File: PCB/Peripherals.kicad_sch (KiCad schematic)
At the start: 0 parts

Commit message: ADD: Ethernet
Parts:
- added J3: USB4216-03-A, USB421603A, symbol SamacSys_Parts:USB4216-03-A
- added J6: SS-90000-009, SS90000009, symbol SamacSys_Parts:SS-90000-009
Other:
- note added: "Ethernet"
- note added: "USB C"

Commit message: Add: Ethernet
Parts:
- added C14, C15, C16, C17, C18, C20: 100nF, CAPC1608X90N, symbol SamacSys_Parts:CC0603KRX7R7BB104
- added C19: 10uF, CAPPM3216X180N, symbol SamacSys_Parts:TAJA106K016R
- added C21: 1uF, CAPC1608X90N, symbol SamacSys_Parts:CC0603KRX5R7BB105
- added C22: 470pF, CAPC1608X90N, symbol SamacSys_Parts:CC0603JRNPO9BN471
- added C23: 1nF, CAPC3216X145N, symbol SamacSys_Parts:CC1206KKX7RDBB102
- added FB1: BEAD, BEADC1608X95N, symbol SamacSys_Parts:FCM1608KF-601T05
- added IC3: LAN8742A-CZ-TR, QFN50P400X400X100-25N-D, symbol SamacSys_Parts:LAN8742A-CZ-TR
- added IC4: USBLC6-4SC6, SOT95P280X145-6N, symbol SamacSys_Parts:USBLC6-4SC6
- added JP4, JP5: Jumper_2_Open, symbol Jumper:Jumper_2_Open
- added R11, R13, R14, R15, R16, R32: 10K, RESC1608X50N, symbol SamacSys_Parts:CRCW060310K0FKEI
- added R17, R18, R19, R20: 33, RESC1608X55N, symbol SamacSys_Parts:CRG0603F33R
- added R21: 1K5, RESC1608X50N, symbol SamacSys_Parts:CRCW06031K50FKED
- added R22: 0, RESC1608X50N, symbol SamacSys_Parts:CRCW06030000Z0EI
- added R23: 12K1, RESC1609X55N, symbol SamacSys_Parts:ERJ-P03F1212V
- added R24, R25, R26, R27: 50, RESC1608X55N, symbol SamacSys_Parts:TNPW060350R0DEEA
- added R28, R29, R30, R31: 75, RESC1608X55N, symbol SamacSys_Parts:RC0603FR-0775RL
- added R33, R34: 270, RESC1608X55N, symbol SamacSys_Parts:RC0603FR-07270RL
- added T1: H1102NL, SOIC127P940X597-16N, symbol SamacSys_Parts:H1102NL
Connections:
- net at J6.1: now also T1.16 (TX+)
- net at J6.10 (A_GREEN): now also IC3.2 (LED2/NINT/NPME/NINTSEL), R32.2
- net at J6.11 (K_YELLOW): now also R34.2
- net at J6.12 (A_YELLOW): now also C14.1, C15.1, C16.2, C17.2, C18.2, C19.1 (+), FB1.2, IC3.19 (VDD1A), IC3.3 (LED1/NINT/NPME/REGOFF), IC4.5 (VBUS), R24.2, R25.2, R26.2, R27.2, T1.2 (CT_1), T1.7 (CT_2)
- net at J6.2: now also T1.14 (TX-)
- net at J6.3: now also T1.11 (RX+)
- net at J6.4: now also J6.5, R29.2, R30.2, T1.15 (NC_6)
- net at J6.6: now also T1.9 (RX-)
- net at J6.7: now also J6.8, R31.2
- net at J6.9 (K_GREEN): now also R33.2
- net GNDPWR: now reaches J6.MH3
- net GNDPWR: now also J6.MH4, C23.1, JP4.1 (A), JP5.1 (A)
- net GNDREF: now reaches J3.A1 (GND_1)
- net GNDREF: now also J3.B1 (GND_2), J3.G1 (GND_3), J3.G2 (GND_4), J3.G3 (GND_5), J3.G4 (GND_6), C14.2, C15.2, C16.1, C17.1, C18.1, C19.2 (-), C20.1, C21.2, C22.2, IC3.25 (EP), IC4.2 (GND), JP4.2 (B), JP5.2 (B), R11.1, R23.2, R32.1, R33.1, R34.1
- net 5V: now reaches J3.A4 (VBUS_1)
- net 5V: now also J3.B4 (VBUS_2)
- new net: IC3.8 (RXD0/MODE0), R14.2, R17.2
- new net: IC3.22 (RXN), IC4.6 (I/O4), R24.1, T1.8 (RD-)
- new net: IC3.11 (CRS_DV/MODE2), R15.2, R19.1
- new net: C23.2, R28.1, R29.1, R30.1, R31.1
- new net: IC3.21 (TXP), IC4.3 (I/O2), R25.1, T1.1 (TD+)
- new net: R28.2, T1.10 (NC_3)
- new net: IC3.20 (TXN), IC4.4 (I/O3), R26.1, T1.3 (TD-)
- new net: IC3.23 (RXP), IC4.1 (I/O1), R27.1, T1.6 (RD+)
- new net: IC3.7 (RXD1/MODE1), R13.2, R18.2
- new net: IC3.10 (RXER/PHYAD0), R11.2
- new net: IC3.14 (NINT/REFCLKO), R16.2, R20.1
- new net: IC3.15 (NRST), R22.1
- new net: IC3.24 (RBIAS), R23.1
- new net: C21.1, C22.1, IC3.6 (VDDCR)
- new net +3V3_PER: C20.2, FB1.1, IC3.9 (VDDIO), R13.1, R14.1, R15.1, R16.1, R21.1
- new net NRST: R22.2
- new net PHY_CLK_25MHZ: IC3.5 (XTAL1/CLKIN)
- new net RMII_CRX_DV: R19.2
- new net RMII_MDC: IC3.13 (MDC)
- new net RMII_MDIO: IC3.12 (MDIO), R21.2
- new net RMII_REF_CLK: R20.2
- new net RMII_RXD0: R17.1
- new net RMII_RXD1: R18.1
- new net RMII_TXD0: IC3.17 (TXD0)
- new net RMII_TXD1: IC3.18 (TXD1)
- new net RMII_TX_EN: IC3.16 (TXEN)
- no-connect marks 0 -> 9
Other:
- note added: "CC1 fait parti de la norme ??"
- note added: "Ne pas oublier pair différentiel !?"
- moved on the sheet: J3, J6

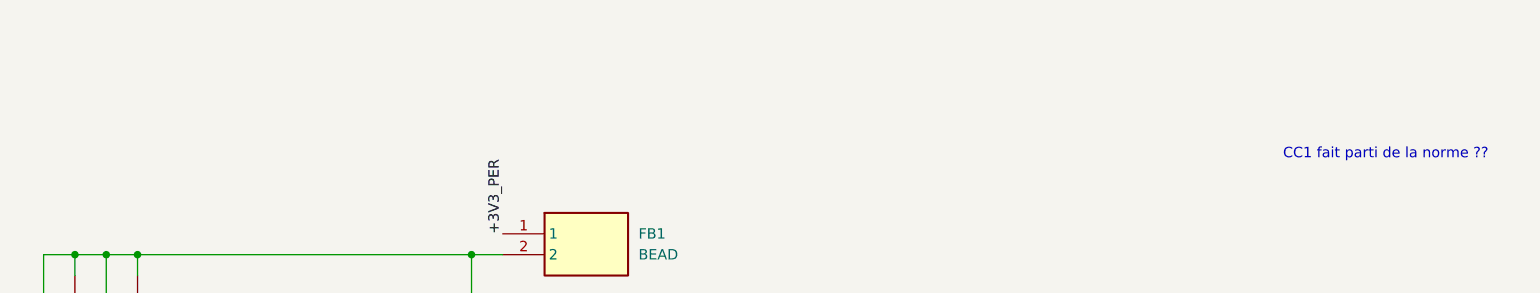
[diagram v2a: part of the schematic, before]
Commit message: List of Modifs:
Corrected power supply sheet
Updated motor driver sheet
Added a project name to a lot of sheets (don't know why...)
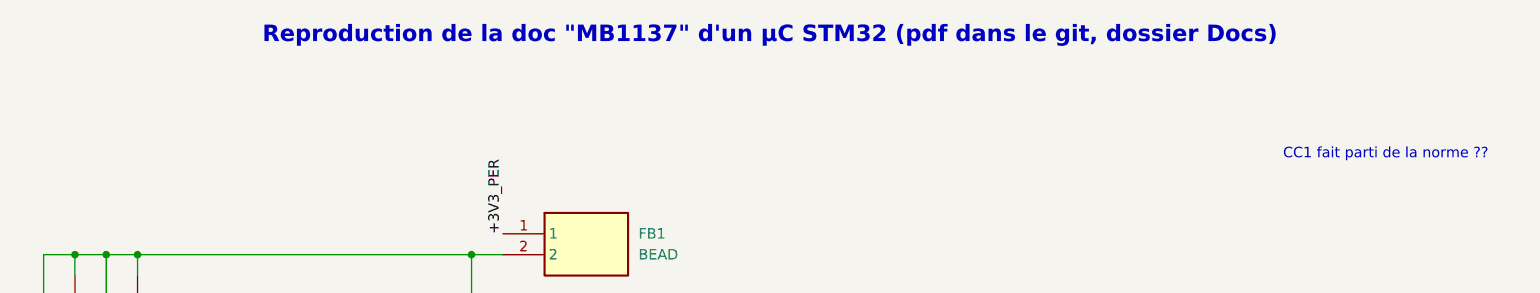
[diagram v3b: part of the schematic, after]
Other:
- note added: "Reproduction de la doc "MB1137" d'un µC STM32 (pdf dans le git, dossier Docs)"
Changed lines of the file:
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@@
 		)
 	)
+	(text "Reproduction de la doc \"MB1137\" d'un µC STM32 (pdf dans le git, dossier Docs)"
+		(exclude_from_sim no)
+		(at 144.272 16.51 0)
+		(effects
+			(font
+				(size 2 2)
+				(thickness 0.6)
+				(bold yes)
+			)
+		)
+	)
 	(text "CC1 fait parti de la norme ??"
 		(exclude_from_sim no)
@@
 		)
 		(instances
-			(project ""
+			(project "PCB"
 				(path "/117fd49e-499d-4b54-b58c-f6b538ecca4a/b9176f6a-4299-4bca-a59b-5ff3df09c616/6ae8cb66-0d01-49c6-940e-175426e825e5"
 					(reference "#PWR037")
@@
 		)
 		(instances
-			(project ""
+			(project "PCB"
 				(path "/117fd49e-499d-4b54-b58c-f6b538ecca4a/b9176f6a-4299-4bca-a59b-5ff3df09c616/6ae8cb66-0d01-49c6-940e-175426e825e5"
 					(reference "R24")
@@
 		)
 		(instances
-			(project ""
+			(project "PCB"
 				(path "/117fd49e-499d-4b54-b58c-f6b538ecca4a/b9176f6a-4299-4bca-a59b-5ff3df09c616/6ae8cb66-0d01-49c6-940e-175426e825e5"
 					(reference "C23")
@@
 		)
 		(instances
-			(project ""
+			(project "PCB"
 				(path "/117fd49e-499d-4b54-b58c-f6b538ecca4a/b9176f6a-4299-4bca-a59b-5ff3df09c616/6ae8cb66-0d01-49c6-940e-175426e825e5"
 					(reference "T1")
@@
 		)
 		(instances
-			(project ""
+			(project "PCB"
 				(path "/117fd49e-499d-4b54-b58c-f6b538ecca4a/b9176f6a-4299-4bca-a59b-5ff3df09c616/6ae8cb66-0d01-49c6-940e-175426e825e5"
 					(reference "IC3")
@@
 		)
 		(instances
-			(project ""
+			(project "PCB"
 				(path "/117fd49e-499d-4b54-b58c-f6b538ecca4a/b9176f6a-4299-4bca-a59b-5ff3df09c616/6ae8cb66-0d01-49c6-940e-175426e825e5"
 					(reference "R21")
@@
 		)
 		(instances
-			(project ""
+			(project "PCB"
 				(path "/117fd49e-499d-4b54-b58c-f6b538ecca4a/b9176f6a-4299-4bca-a59b-5ff3df09c616/6ae8cb66-0d01-49c6-940e-175426e825e5"
 					(reference "#PWR044")
@@
 		)
 		(instances
-			(project ""
+			(project "PCB"
 				(path "/117fd49e-499d-4b54-b58c-f6b538ecca4a/b9176f6a-4299-4bca-a59b-5ff3df09c616/6ae8cb66-0d01-49c6-940e-175426e825e5"
 					(reference "C21")
@@
 		)
 		(instances
-			(project ""
+			(project "PCB"
 				(path "/117fd49e-499d-4b54-b58c-f6b538ecca4a/b9176f6a-4299-4bca-a59b-5ff3df09c616/6ae8cb66-0d01-49c6-940e-175426e825e5"
 					(reference "J6")
@@
 		)
 		(instances
-			(project ""
+			(project "PCB"
 				(path "/117fd49e-499d-4b54-b58c-f6b538ecca4a/b9176f6a-4299-4bca-a59b-5ff3df09c616/6ae8cb66-0d01-49c6-940e-175426e825e5"
 					(reference "R17")
@@
 		)
 		(instances
-			(project ""
+			(project "PCB"
 				(path "/117fd49e-499d-4b54-b58c-f6b538ecca4a/b9176f6a-4299-4bca-a59b-5ff3df09c616/6ae8cb66-0d01-49c6-940e-175426e825e5"
 					(reference "FB1")
@@
 		)
 		(instances
-			(project ""
+			(project "PCB"
 				(path "/117fd49e-499d-4b54-b58c-f6b538ecca4a/b9176f6a-4299-4bca-a59b-5ff3df09c616/6ae8cb66-0d01-49c6-940e-175426e825e5"
 					(reference "IC4")
@@
 		)
 		(instances
-			(project ""
+			(project "PCB"
 				(path "/117fd49e-499d-4b54-b58c-f6b538ecca4a/b9176f6a-4299-4bca-a59b-5ff3df09c616/6ae8cb66-0d01-49c6-940e-175426e825e5"
 					(reference "R22")
@@
 		)
 		(instances
-			(project ""
+			(project "PCB"
 				(path "/117fd49e-499d-4b54-b58c-f6b538ecca4a/b9176f6a-4299-4bca-a59b-5ff3df09c616/6ae8cb66-0d01-49c6-940e-175426e825e5"
 					(reference "JP4")
@@
 		)
 		(instances
-			(project ""
+			(project "PCB"
 				(path "/117fd49e-499d-4b54-b58c-f6b538ecca4a/b9176f6a-4299-4bca-a59b-5ff3df09c616/6ae8cb66-0d01-49c6-940e-175426e825e5"
 					(reference "C22")
@@
 		)
 		(instances
-			(project ""
+			(project "PCB"
 				(path "/117fd49e-499d-4b54-b58c-f6b538ecca4a/b9176f6a-4299-4bca-a59b-5ff3df09c616/6ae8cb66-0d01-49c6-940e-175426e825e5"
 					(reference "J3")
@@
 		)
 		(instances
-			(project ""
+			(project "PCB"
 				(path "/117fd49e-499d-4b54-b58c-f6b538ecca4a/b9176f6a-4299-4bca-a59b-5ff3df09c616/6ae8cb66-0d01-49c6-940e-175426e825e5"
 					(reference "R23")
@@
 		)
 		(instances
-			(project ""
+			(project "PCB"
 				(path "/117fd49e-499d-4b54-b58c-f6b538ecca4a/b9176f6a-4299-4bca-a59b-5ff3df09c616/6ae8cb66-0d01-49c6-940e-175426e825e5"
 					(reference "R33")
@@
 		)
 		(instances
-			(project ""
+			(project "PCB"
 				(path "/117fd49e-499d-4b54-b58c-f6b538ecca4a/b9176f6a-4299-4bca-a59b-5ff3df09c616/6ae8cb66-0d01-49c6-940e-175426e825e5"
 					(reference "C19")
@@
 		)
 		(instances
-			(project ""
+			(project "PCB"
 				(path "/117fd49e-499d-4b54-b58c-f6b538ecca4a/b9176f6a-4299-4bca-a59b-5ff3df09c616/6ae8cb66-0d01-49c6-940e-175426e825e5"
 					(reference "R28")
@@
 		)
 		(instances
-			(project ""
+			(project "PCB"
 				(path "/117fd49e-499d-4b54-b58c-f6b538ecca4a/b9176f6a-4299-4bca-a59b-5ff3df09c616/6ae8cb66-0d01-49c6-940e-175426e825e5"
 					(reference "#PWR046")
@@
 		)
 		(instances
-			(project ""
+			(project "PCB"
 				(path "/117fd49e-499d-4b54-b58c-f6b538ecca4a/b9176f6a-4299-4bca-a59b-5ff3df09c616/6ae8cb66-0d01-49c6-940e-175426e825e5"
 					(reference "C14")

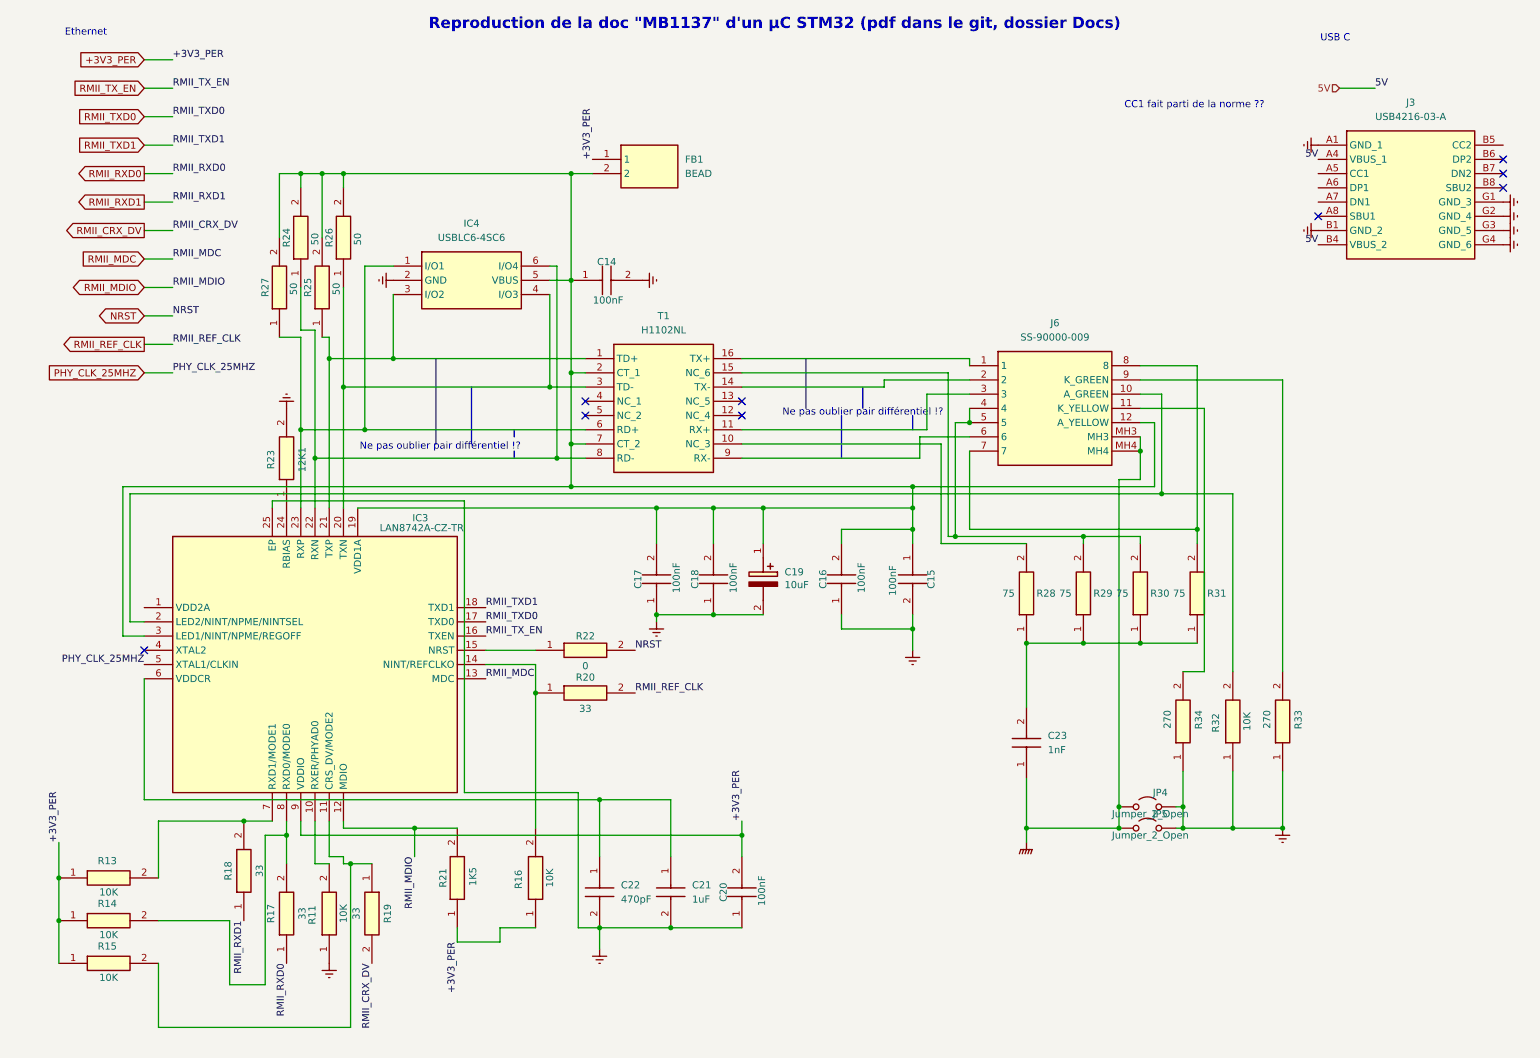
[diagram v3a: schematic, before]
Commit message: Updated MCU sheet
Added decoupling capacitors
Linked Ethernet to MCU
Started Usb linking to MCU
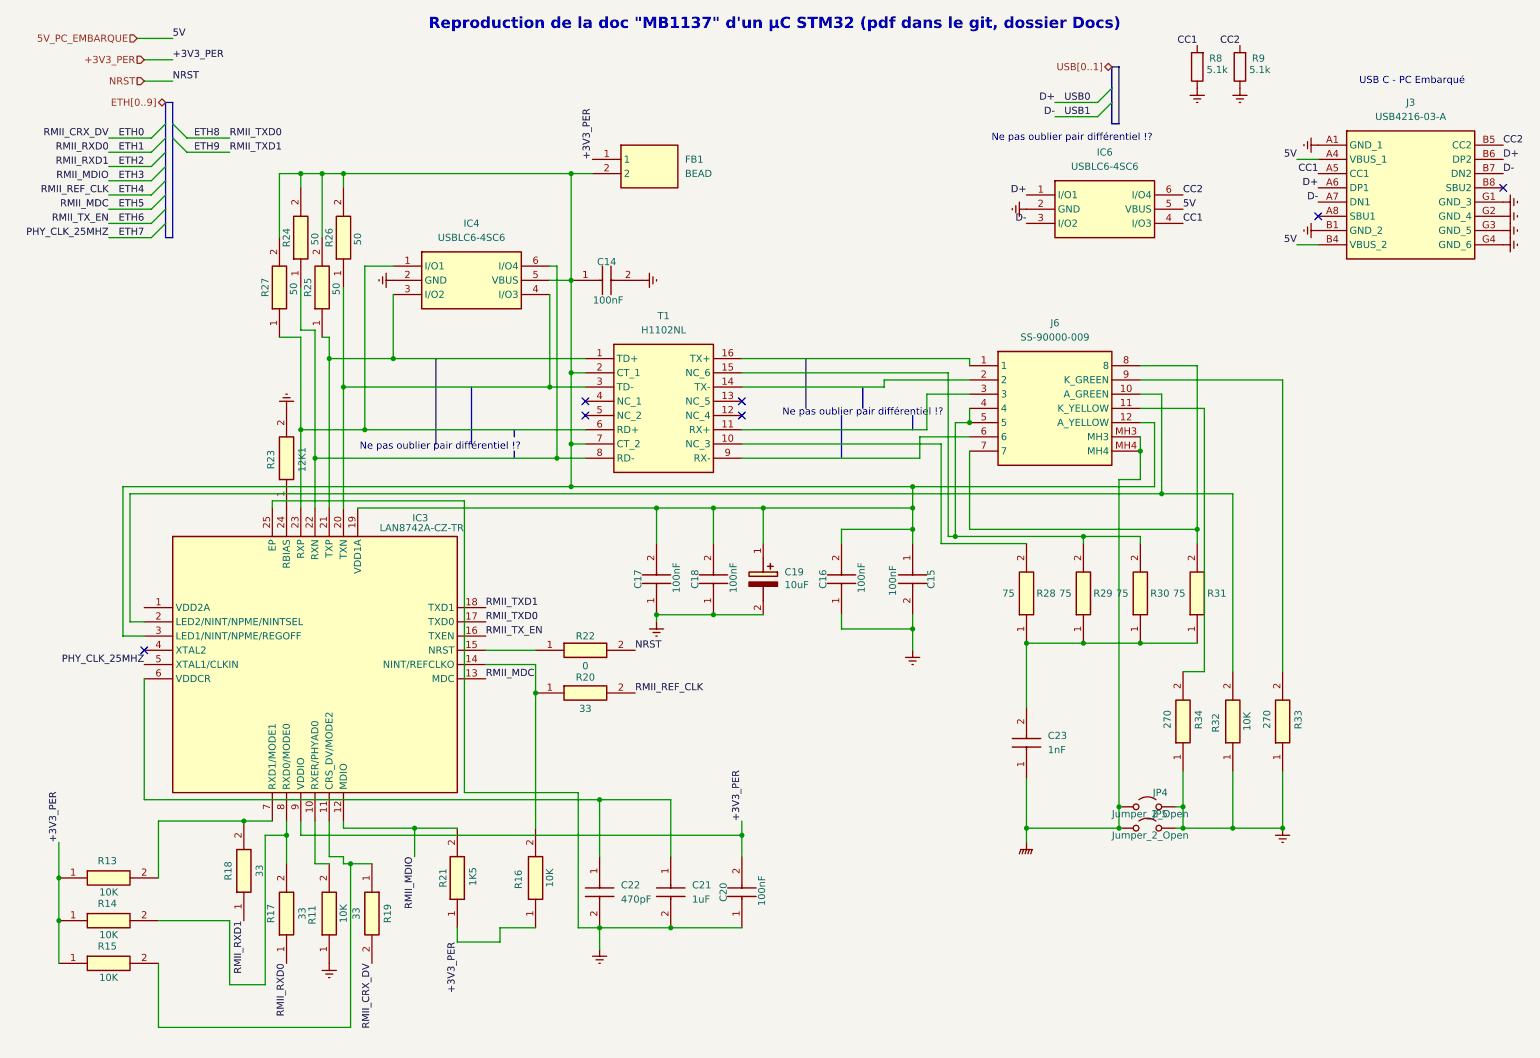
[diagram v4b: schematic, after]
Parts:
- added IC6: USBLC6-4SC6, SOT95P280X145-6N, symbol SamacSys_Parts:USBLC6-4SC6
- added R8, R9: 5.1k, symbol Device:R
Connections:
- net GNDREF: now also IC6.2 (GND), R8.1, R9.1
- net CC1: now reaches J3.A5 (CC1)
- net CC1: now also IC6.4 (I/O3), R8.2
- net D+: now reaches J3.A6 (DP1)
- net D+: now also J3.B6 (DP2), IC6.1 (I/O1)
- net D-: now reaches J3.A7 (DN1)
- net D-: now also J3.B7 (DN2), IC6.3 (I/O2)
- net CC2: now reaches J3.B5 (CC2)
- net CC2: now also IC6.6 (I/O4), R9.2
- net 5V renamed 5V_PC_EMBARQUE
- net 5V_PC_EMBARQUE: now also IC6.5 (VBUS)
- net PHY_CLK_25MHZ renamed ETH7
- net RMII_CRX_DV renamed ETH0
- net RMII_MDC renamed ETH5
- net RMII_MDIO renamed ETH3
- net RMII_REF_CLK renamed ETH4
- net RMII_RXD0 renamed ETH1
- net RMII_RXD1 renamed ETH2
- net RMII_TXD0 renamed ETH8
- net RMII_TXD1 renamed ETH9
- net RMII_TX_EN renamed ETH6
- no-connect marks 9 -> 7
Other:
- note added: "USB C - PC Embarqué"
- note removed: "CC1 fait parti de la norme ??"
- note removed: "Ethernet"
- note removed: "USB C"
